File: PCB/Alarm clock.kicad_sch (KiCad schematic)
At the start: 4 parts, among them J1 TFT, J2 Conn_01x06_Female, SW1 SW_MEC_5G, U1 ESP32-C3_SUPERMINI

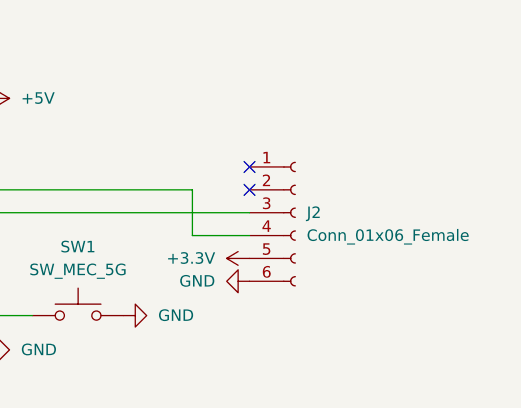
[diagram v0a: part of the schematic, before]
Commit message: Use Hardware SPI and start working on SD support
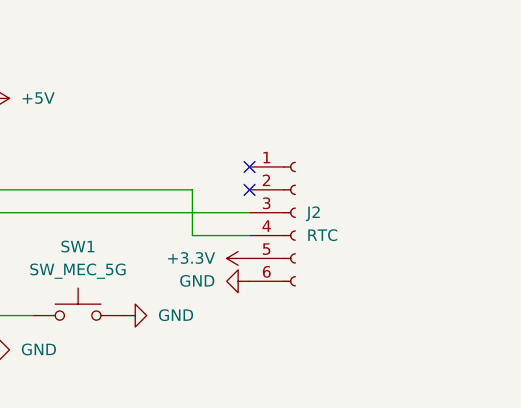
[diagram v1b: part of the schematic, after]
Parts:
- J2: value Conn_01x06_Female -> RTC
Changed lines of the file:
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@@
       (effects (font (size 1.27 1.27)) (justify left))
     )
-    (property "Value" "Conn_01x06_Female" (id 1) (at 200.66 93.9799 0)
+    (property "Value" "RTC" (id 1) (at 200.66 93.9799 0)
       (effects (font (size 1.27 1.27)) (justify left))
     )
@@
     )
     (path "/8d2649af-c4b5-4d1d-a8b0-0c4d99b42cd3"
-      (reference "J2") (unit 1) (value "Conn_01x06_Female") (footprint "Connector_PinHeader_2.54mm:PinHeader_1x06_P2.54mm_Vertical")
+      (reference "J2") (unit 1) (value "RTC") (footprint "Connector_PinHeader_2.54mm:PinHeader_1x06_P2.54mm_Vertical")
     )
     (path "/8ce9953c-27b5-4d7b-a939-7c7cb3c846e3"

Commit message: PCB Update
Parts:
- removed SW1: SW_MEC_5G, Button_Switch_SMD:SW_MEC_5GSH9, symbol Switch:SW_MEC_5G
- added SW1: SW_Push, Button_Switch_THT:SW_PUSH_6mm, symbol Switch:SW_Push
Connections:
- net GND: now also SW1.2
- net at U1.10 (GPIO10): now also SW1.1
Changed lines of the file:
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@@
     (pin "1")
+  )
+  (symbol (lib_id "Switch:SW_Push") (at 175.26 102.87 0) (unit 1)
+    (in_bom yes) (on_board yes) (fields_autoplaced)
+    (property "Reference" "SW1" (id 0) (at 175.26 95.25 0))
+    (property "Value" "SW_Push" (id 1) (at 175.26 97.79 0))
+    (property "Footprint" "Button_Switch_THT:SW_PUSH_6mm" (id 2) (at 175.26 97.79 0)
+      (effects (font (size 1.27 1.27)) hide)
+    )
+    (property "Datasheet" "~" (id 3) (at 175.26 97.79 0)
+      (effects (font (size 1.27 1.27)) hide)
+    )
+    (pin "1")
+    (pin "2")
   )
   (symbol (lib_id "ESP32-C3_SUPERMINI:ESP32-C3_SUPERMINI") (at 147.32 91.44 0) (unit 1)
@@
     (pin "1")
   )
-  (symbol (lib_id "Switch:SW_MEC_5G") (at 175.26 102.87 0) (unit 1)
-    (in_bom yes) (on_board yes) (fields_autoplaced)
-    (property "Reference" "SW1" (id 0) (at 175.26 95.25 0))
-    (property "Value" "SW_MEC_5G" (id 1) (at 175.26 97.79 0))
-    (property "Footprint" "Button_Switch_SMD:SW_MEC_5GSH9" (id 2) (at 175.26 97.79 0)
-      (effects (font (size 1.27 1.27)) hide)
-    )
-    (property "Datasheet" "http://www.apem.com/int/index.php?controller=attachment&id_attachment=488" (id 3) (at 175.26 97.79 0)
-      (effects (font (size 1.27 1.27)) hide)
-    )
-    (pin "1")
-    (pin "3")
-    (pin "2")
-    (pin "4")
-  )
   (symbol (lib_id "Connector:Conn_01x06_Female") (at 199.39 91.44 0) (unit 1)
     (in_bom yes) (on_board yes) (fields_autoplaced)
@@
       (reference "J2") (unit 1) (value "RTC") (footprint "Connector_PinHeader_2.54mm:PinHeader_1x06_P2.54mm_Vertical")
     )
-    (path "/8ce9953c-27b5-4d7b-a939-7c7cb3c846e3"
-      (reference "SW1") (unit 1) (value "SW_MEC_5G") (footprint "Button_Switch_SMD:SW_MEC_5GSH9")
+    (path "/50e6b88c-1bd3-4928-86fd-758de4de04a3"
+      (reference "SW1") (unit 1) (value "SW_Push") (footprint "Button_Switch_THT:SW_PUSH_6mm")
     )
     (path "/78739525-b736-4a0a-8df7-5c681a01d0c1"
